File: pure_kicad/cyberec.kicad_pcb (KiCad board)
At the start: 4 copper layers, 50 x 50 mm, 89 parts, among them J1 XT60M, J2 XT60M, J3 XT60M, J4 XT60M, J5 Conn_01x04_Pin, J6 Conn_01x04_Pin, Q1 Q_NMOS_DGS, Q2 Q_NMOS_DGS, Q3 Q_NMOS_DGS, Q4 Q_NMOS_DGS, Q5 Q_PMOS_SGD, Q6 Q_NMOS_DGS, Q7 Q_NMOS_DGS, U1 BQ25756ERRVR, U2 BQ40Z80RSMR

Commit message: Layout starting to look alright
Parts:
- C15, C19, C20, C21, C22, C29, C30, C31, C32, C33, C7, D10, R18, R29: moved to B.Cu
- D9, R26, R27, R28: moved to F.Cu
- R16: footprint Resistor_SMD:R_0402_1005Metric_Pad0.72x0.64mm_HandSolder -> Resistor_SMD:R_0603_1608Metric_Pad0.98x0.95mm_HandSolder
- moved C24 54.5 mm to (81.0, 94.7)
- moved C28 51.7 mm to (81.1, 79.7)
- moved C23 51.3 mm to (81.0, 97.7)
- moved C27 50.0 mm to (81.0, 82.7)
- moved J5 49.1 mm to (77.8, 99.2), turned to 90 degrees
- moved C25 48.8 mm to (81.0, 91.7)
- moved C15 48.4 mm to (96.6, 92.8), turned to 180 degrees
- moved C26 47.4 mm to (81.0, 88.7)
- moved J3 45.5 mm to (121.6, 94.6)
- moved J4 45.5 mm to (121.6, 78.4)
- moved J6 44.8 mm to (77.8, 85.2), turned to 90 degrees
- moved R19 43.4 mm to (81.1, 99.2)
- moved C31 41.2 mm to (85.0, 92.7), turned to 90 degrees
- moved R25 41.0 mm to (81.1, 81.2)
- moved R20 41.0 mm to (81.1, 96.2)
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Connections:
- C15 pad 1: unconnected-(C15-Pad1) -> VAC
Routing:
- net VAC: track 0.00 -> 17.3 mm
- net /Charger/SRN: track 0.00 -> 15.0 mm
- net /Charger/SRP: track 0.00 -> 14.3 mm
- net Net-(U2-VC2): track 0.00 -> 14.1 mm
- net Net-(U2-VC6): track 0.00 -> 14.0 mm
- net Net-(U2-VC5): track 0.00 -> 13.5 mm
- net /Charger/ACP: track 0.00 -> 13.5 mm
- net Net-(U2-VC1): track 0.00 -> 13.3 mm
- net /Charger/ACN: track 0.00 -> 12.2 mm
- net Net-(U2-VC4): track 0.00 -> 11.7 mm
- net Net-(U2-VC3): track 0.00 -> 10.4 mm
- net /Charger/SW1: track 0.00 -> 8.85 mm
- net /Battery Monitor/LED_A: track 0.00 -> 8.22 mm
- net /Charger/FBG: track 0.00 -> 7.86 mm
- net Net-(U2-BAT): track 0.00 -> 7.67 mm
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- added copper zone on In1.Cu, net Earth

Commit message: Do most top side zones
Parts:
- C1, C10, C15, C18, C19, C2, C20, C21, C22, C23, C24, C25, C26, C27, C28, C29, C3, C30, C31, C32, C33, C4, C5, C6, C7, C8, C9: footprint Capacitor_SMD:C_0603_1608Metric_Pad1.08x0.95mm_HandSolder -> cyberec:C_0603_1608Metric_Pad1.08x0.95mm_HandSolder
- C11, C12, C14, C16, C17: footprint Capacitor_SMD:CP_Elec_10x14.3 -> cyberec:CP_Elec_10x14.3
- C13, C34: footprint Capacitor_SMD:C_0603_1608Metric_Pad1.08x0.95mm_HandSolder -> cyberec:C_0603_1608Metric_Pad1.08x0.95mm_HandSolder; moved to B.Cu
- D1, D2: footprint Diode_SMD:D_SMA_Handsoldering -> cyberec:D_SOD-882D
- D10: footprint Diode_SMD:D_SMA_Handsoldering -> cyberec:D_SMA_Handsoldering; moved to F.Cu
- D3, D4, D5, D6, D7, D8: footprint LED_SMD:LED_0603_1608Metric_Pad1.05x0.95mm_HandSolder -> cyberec:LED_0603_1608Metric_Pad1.05x0.95mm_HandSolder
- D9: footprint Diode_SMD:D_SMA_Handsoldering -> cyberec:D_SMA_Handsoldering
- J1, J2, J3, J4: footprint Connector_AMASS:AMASS_XT60-M_1x02_P7.20mm_Vertical -> cyberec:AMASS_XT60-M_1x02_P7.20mm_Vertical
- J5, J6: footprint Connector_JST:JST_XH_B4B-XH-A_1x04_P2.50mm_Vertical -> cyberec:JST_XH_B4B-XH-A_1x04_P2.50mm_Vertical
- R1, R10, R11, R12, R13, R15, R16, R18, R19, R2, R20, R21, R23, R24, R25, R29, R5, R6, R7, R8, R9: footprint Resistor_SMD:R_0603_1608Metric_Pad0.98x0.95mm_HandSolder -> cyberec:R_0603_1608Metric_Pad0.98x0.95mm_HandSolder
- R14, R26, R27, R28: footprint Resistor_SMD:R_0402_1005Metric_Pad0.72x0.64mm_HandSolder -> cyberec:R_0402_1005Metric_Pad0.72x0.64mm_HandSolder
- R22: footprint Resistor_SMD:R_1210_3225Metric_Pad1.30x2.65mm_HandSolder -> cyberec:R_1210_3225Metric_Pad1.30x2.65mm_HandSolder
- moved D9 21.3 mm to (112.2, 104.2), turned to 180 degrees
- moved C34 19.9 mm to (88.5, 89.8), turned to 180 degrees
- moved D10 17.7 mm to (115.2, 90.8), turned to -90 degrees
- moved C13 11.2 mm to (94.5, 86.6)
- moved R5 9.06 mm to (82.8, 103.6), turned to 0 degrees
- moved R22 8.84 mm to (110.5, 88.2), turned to 0 degrees
- moved R1 8.68 mm to (82.8, 105.4), turned to 0 degrees
- moved C3 5.02 mm to (85.5, 104.5), turned to 90 degrees
- moved R27 3.25 mm to (112.8, 93.5)
- moved R26 2.90 mm to (112.8, 96.8)
- moved C5 2.74 mm to (88.3, 103.6), turned to 0 degrees
- moved Q6 2.30 mm to (115.2, 98.7)
- moved Q5 2.30 mm to (110.4, 93.5)
- moved Q7 2.30 mm to (110.2, 99.0)
- moved R28 1.25 mm to (112.8, 101.0)
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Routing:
- net /Charger/ACP: track 13.5 -> 0.00 mm
- net /Charger/ACN: track 12.2 -> 0.00 mm
- net /Charger/SW1: track 8.85 -> 0.00 mm
- net VAC: track 17.3 -> 25.6 mm
- net /Battery Monitor/DSG: track 0.00 -> 6.24 mm
- net VCC: track 0.00 -> 4.19 mm
- net /Battery Monitor/CHG: track 0.00 -> 3.62 mm
- net /Battery Monitor/PCHG: track 0.00 -> 1.83 mm
- net Net-(D10-K): track 1.27 -> 0.00 mm
- net Net-(C1-Pad2): track 4.72 -> 3.75 mm
- net Net-(C3-Pad2): track 4.68 -> 3.75 mm
- net Net-(C2-Pad2): track 4.39 -> 3.50 mm
- net Net-(C4-Pad2): track 4.29 -> 3.50 mm
- net Earth: vias 0 -> 6
- added copper zone on F.Cu, net +BATT
- added copper zone on F.Cu, net /Charger/SW1
- added copper zone on F.Cu, net /Charger/SW2
- added copper zone on F.Cu, net Earth
- added copper zone on F.Cu, net Net-(Q5-D)
- added copper zone on F.Cu, net VAC
- added copper zone on F.Cu, net VCC
- added copper zone on F.Cu, net VDD
- added copper zone on F.Cu, net VDDA
- added copper zone on F.Cu, net VDDF
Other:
- outline, holes or cut-outs redrawn

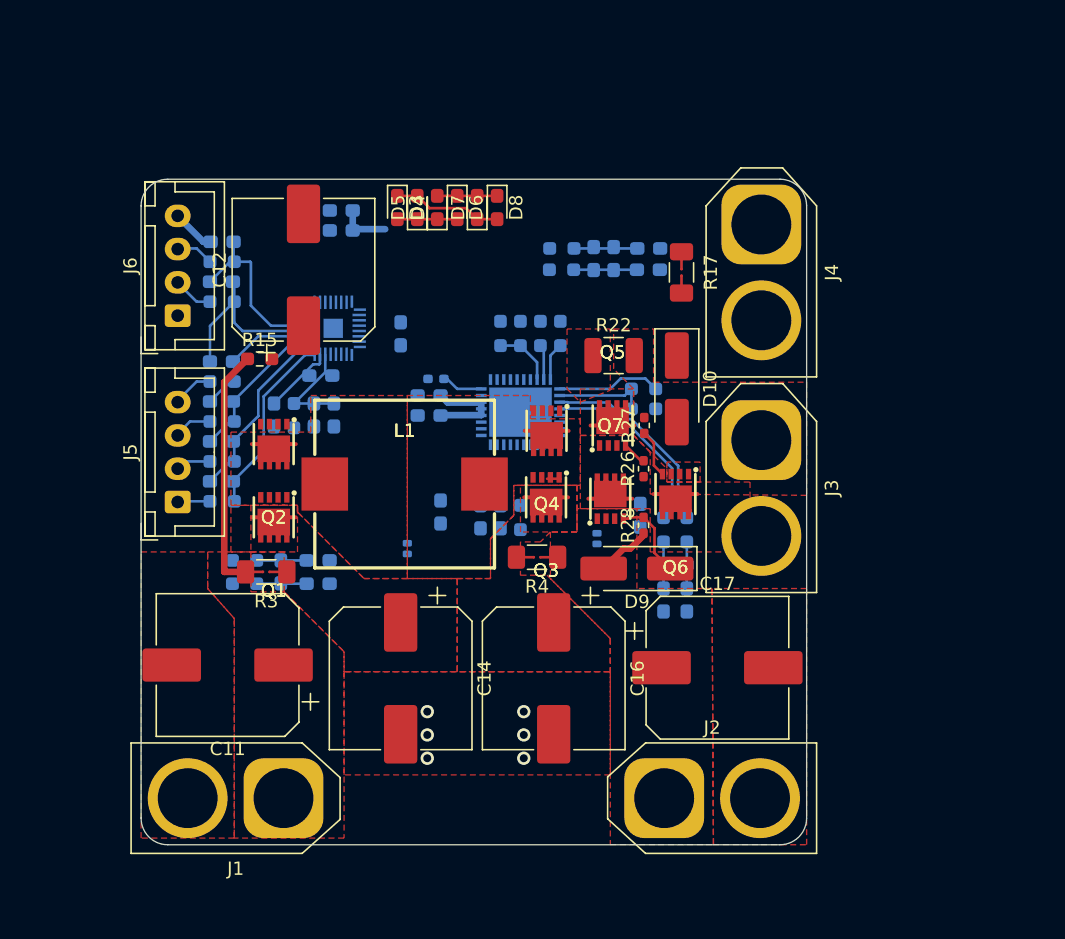
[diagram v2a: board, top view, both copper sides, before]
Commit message: It seems that the charger needs to move.
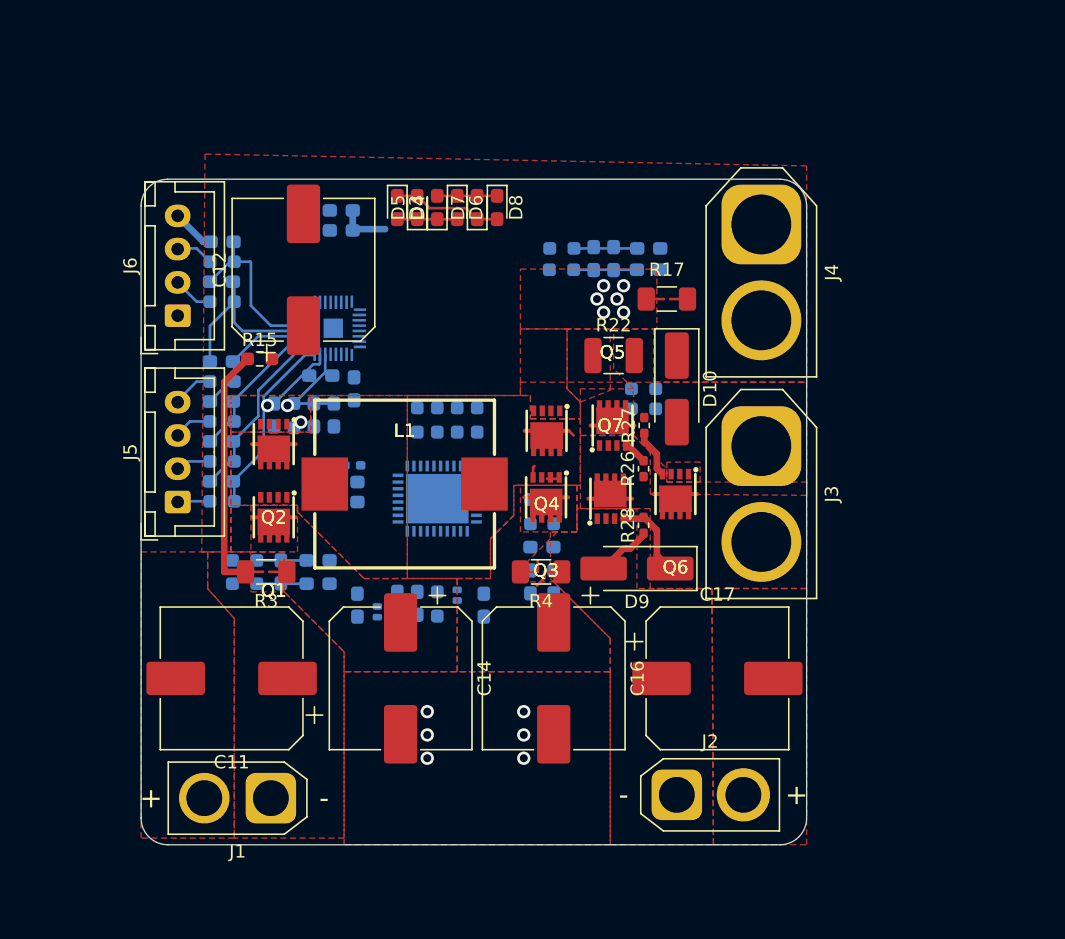
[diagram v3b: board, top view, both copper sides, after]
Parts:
- D1, D2: value D_Schottky -> PMEG2010BELD
- J1: value XT60M -> XT30M; footprint cyberec:AMASS_XT60-M_1x02_P7.20mm_Vertical -> cyberec:AMASS_XT30U-M_1x02_P5.0mm_Vertical
- J2: value XT60M -> XT30F; footprint cyberec:AMASS_XT60-M_1x02_P7.20mm_Vertical -> cyberec:AMASS_XT30U-F_1x02_P5.0mm_Vertical
- moved C8 13.6 mm to (100.8, 107.0)
- moved D2 11.3 mm to (98.8, 106.2), turned to 90 degrees
- moved R2 10.1 mm to (104.2, 100.0)
- moved R6 10.1 mm to (106.0, 100.0)
- moved C2 10.1 mm to (104.2, 105.2)
- moved C4 10.1 mm to (105.1, 102.6)
- moved C6 10.1 mm to (106.0, 105.2)
- moved C7 9.38 mm to (91.2, 107.0), turned to -90 degrees
- moved C10 9.02 mm to (94.2, 106.9)
- moved C15 9.02 mm to (90.4, 99.2)
- moved C18 9.02 mm to (90.4, 97.8)
- moved C9 9.02 mm to (95.8, 106.9)
- moved R10 9.02 mm to (97.2, 93.1)
- moved R13 9.02 mm to (97.2, 106.9)
- moved R14 9.02 mm to (90.9, 96.5)
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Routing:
- net /Charger/SRN: track 15.0 -> 0.00 mm
- net /Charger/SRP: track 14.3 -> 0.00 mm
- net /Charger/FBG: track 7.86 -> 0.00 mm
- net VAC: track 25.6 -> 18.3 mm
- net /Charger/FB: track 7.10 -> 0.00 mm
- net TS_Charge: track 4.57 -> 0.00 mm
- net Net-(U1B-FSW_SYNC): track 3.12 -> 0.00 mm
- net Net-(U1A-ILIM_HIZ): track 2.86 -> 0.00 mm
- net Net-(C2-Pad2): track 3.50 -> 0.83 mm
- net Net-(U1A-ICHG): track 2.66 -> 0.00 mm
- net Net-(C4-Pad2): track 3.50 -> 1.28 mm
- net /Charger/HIDRV2: track 0.00 -> 0.90 mm
- net /Charger/SW2: track 1.02 -> 1.89 mm
- net Net-(D10-K): vias 0 -> 1
- net Earth: vias 6 -> 14
- added copper zone on F.Cu, net -BATT

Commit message: So, 10u X5Rs are a thing. Just use 40 of them
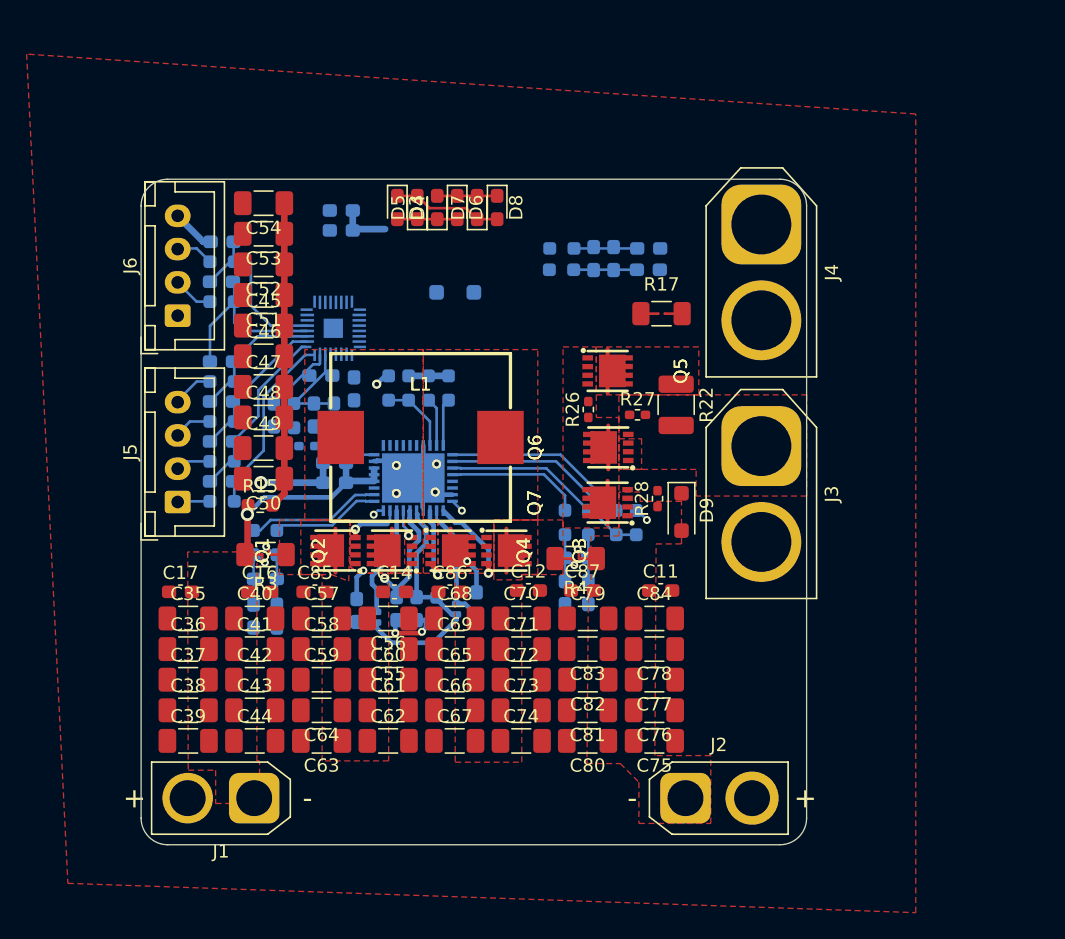
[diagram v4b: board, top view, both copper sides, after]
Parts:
- added C35: 10uF, cyberec:C_1206_3216Metric_Pad1.33x1.80mm_HandSolder, F.Cu at (78.5, 108.0)
- added C36: 10uF, cyberec:C_1206_3216Metric_Pad1.33x1.80mm_HandSolder, F.Cu at (78.5, 110.3)
- added C37: 10uF, cyberec:C_1206_3216Metric_Pad1.33x1.80mm_HandSolder, F.Cu at (78.5, 112.6)
- added C38: 10uF, cyberec:C_1206_3216Metric_Pad1.33x1.80mm_HandSolder, F.Cu at (78.5, 114.9)
- added C39: 10uF, cyberec:C_1206_3216Metric_Pad1.33x1.80mm_HandSolder, F.Cu at (78.5, 117.2)
- added C40: 10uF, cyberec:C_1206_3216Metric_Pad1.33x1.80mm_HandSolder, F.Cu at (83.5, 108.0)
- added C41: 10uF, cyberec:C_1206_3216Metric_Pad1.33x1.80mm_HandSolder, F.Cu at (83.5, 110.3)
- added C42: 10uF, cyberec:C_1206_3216Metric_Pad1.33x1.80mm_HandSolder, F.Cu at (83.5, 112.6)
- added C43: 10uF, cyberec:C_1206_3216Metric_Pad1.33x1.80mm_HandSolder, F.Cu at (83.5, 114.9)
- added C44: 10uF, cyberec:C_1206_3216Metric_Pad1.33x1.80mm_HandSolder, F.Cu at (83.5, 117.2)
- added C45: 10uF, cyberec:C_1206_3216Metric_Pad1.33x1.80mm_HandSolder, F.Cu at (84.2, 86.0)
- added C46: 10uF, cyberec:C_1206_3216Metric_Pad1.33x1.80mm_HandSolder, F.Cu at (84.2, 88.3)
- added C47: 10uF, cyberec:C_1206_3216Metric_Pad1.33x1.80mm_HandSolder, F.Cu at (84.2, 90.6)
- added C48: 10uF, cyberec:C_1206_3216Metric_Pad1.33x1.80mm_HandSolder, F.Cu at (84.2, 92.9)
- added C49: 10uF, cyberec:C_1206_3216Metric_Pad1.33x1.80mm_HandSolder, F.Cu at (84.2, 95.2)
- added C50: 10uF, cyberec:C_1206_3216Metric_Pad1.33x1.80mm_HandSolder, F.Cu at (84.2, 97.5)
- added C51: 10uF, cyberec:C_1206_3216Metric_Pad1.33x1.80mm_HandSolder, F.Cu at (84.2, 83.7)
- added C52: 10uF, cyberec:C_1206_3216Metric_Pad1.33x1.80mm_HandSolder, F.Cu at (84.2, 81.4)
- added C53: 10uF, cyberec:C_1206_3216Metric_Pad1.33x1.80mm_HandSolder, F.Cu at (84.2, 79.1)
- added C54: 10uF, cyberec:C_1206_3216Metric_Pad1.33x1.80mm_HandSolder, F.Cu at (84.2, 76.8)
- added C55: 10uF, cyberec:C_1206_3216Metric_Pad1.33x1.80mm_HandSolder, F.Cu at (93.6, 110.3)
- added C56: 10uF, cyberec:C_1206_3216Metric_Pad1.33x1.80mm_HandSolder, F.Cu at (93.6, 108.0)
- added C57: 10uF, cyberec:C_1206_3216Metric_Pad1.33x1.80mm_HandSolder, F.Cu at (88.6, 108.0)
- added C58: 10uF, cyberec:C_1206_3216Metric_Pad1.33x1.80mm_HandSolder, F.Cu at (88.6, 110.3)
- added C59: 10uF, cyberec:C_1206_3216Metric_Pad1.33x1.80mm_HandSolder, F.Cu at (88.6, 112.6)
- added C60: 10uF, cyberec:C_1206_3216Metric_Pad1.33x1.80mm_HandSolder, F.Cu at (93.6, 112.6)
- added C61: 10uF, cyberec:C_1206_3216Metric_Pad1.33x1.80mm_HandSolder, F.Cu at (93.6, 114.9)
- added C62: 10uF, cyberec:C_1206_3216Metric_Pad1.33x1.80mm_HandSolder, F.Cu at (93.6, 117.2)
- added C63: 10uF, cyberec:C_1206_3216Metric_Pad1.33x1.80mm_HandSolder, F.Cu at (88.6, 117.2)
- added C64: 10uF, cyberec:C_1206_3216Metric_Pad1.33x1.80mm_HandSolder, F.Cu at (88.6, 114.9)
- added C65: 10uF, cyberec:C_1206_3216Metric_Pad1.33x1.80mm_HandSolder, F.Cu at (98.6, 112.6)
- added C66: 10uF, cyberec:C_1206_3216Metric_Pad1.33x1.80mm_HandSolder, F.Cu at (98.6, 114.9)
- added C67: 10uF, cyberec:C_1206_3216Metric_Pad1.33x1.80mm_HandSolder, F.Cu at (98.6, 117.2)
- added C68: 10uF, cyberec:C_1206_3216Metric_Pad1.33x1.80mm_HandSolder, F.Cu at (98.6, 108.0)
- added C69: 10uF, cyberec:C_1206_3216Metric_Pad1.33x1.80mm_HandSolder, F.Cu at (98.6, 110.3)
- added C70: 10uF, cyberec:C_1206_3216Metric_Pad1.33x1.80mm_HandSolder, F.Cu at (103.6, 108.0)
- added C71: 10uF, cyberec:C_1206_3216Metric_Pad1.33x1.80mm_HandSolder, F.Cu at (103.6, 110.3)
- added C72: 10uF, cyberec:C_1206_3216Metric_Pad1.33x1.80mm_HandSolder, F.Cu at (103.6, 112.6)
- added C73: 10uF, cyberec:C_1206_3216Metric_Pad1.33x1.80mm_HandSolder, F.Cu at (103.6, 114.9)
- added C74: 10uF, cyberec:C_1206_3216Metric_Pad1.33x1.80mm_HandSolder, F.Cu at (103.6, 117.2)
- added C75: 10uF, cyberec:C_1206_3216Metric_Pad1.33x1.80mm_HandSolder, F.Cu at (113.6, 117.2)
- added C76: 10uF, cyberec:C_1206_3216Metric_Pad1.33x1.80mm_HandSolder, F.Cu at (113.6, 114.9)
- added C77: 10uF, cyberec:C_1206_3216Metric_Pad1.33x1.80mm_HandSolder, F.Cu at (113.6, 112.6)
- added C78: 10uF, cyberec:C_1206_3216Metric_Pad1.33x1.80mm_HandSolder, F.Cu at (113.6, 110.3)
- added C79: 10uF, cyberec:C_1206_3216Metric_Pad1.33x1.80mm_HandSolder, F.Cu at (108.6, 108.0)
- added C80: 10uF, cyberec:C_1206_3216Metric_Pad1.33x1.80mm_HandSolder, F.Cu at (108.5, 117.2)
- added C81: 10uF, cyberec:C_1206_3216Metric_Pad1.33x1.80mm_HandSolder, F.Cu at (108.5, 114.9)
- added C82: 10uF, cyberec:C_1206_3216Metric_Pad1.33x1.80mm_HandSolder, F.Cu at (108.6, 112.6)
- added C83: 10uF, cyberec:C_1206_3216Metric_Pad1.33x1.80mm_HandSolder, F.Cu at (108.5, 110.3)
- added C84: 10uF, cyberec:C_1206_3216Metric_Pad1.33x1.80mm_HandSolder, F.Cu at (113.6, 108.0)
- added C85: 100nF, cyberec:C_0603_1608Metric_Pad1.08x0.95mm_HandSolder, F.Cu at (88.1, 106.0)
- added C86: 100nF, cyberec:C_0603_1608Metric_Pad1.08x0.95mm_HandSolder, F.Cu at (98.2, 106.0)
- added C87: 100nF, cyberec:C_0603_1608Metric_Pad1.08x0.95mm_HandSolder, F.Cu at (108.2, 105.9)
- C11, C12, C14, C16: value 82uF -> 1uF; footprint cyberec:CP_Elec_10x14.3 -> cyberec:C_0603_1608Metric_Pad1.08x0.95mm_HandSolder
- C17: value 82uF -> 100nF; footprint cyberec:CP_Elec_10x14.3 -> cyberec:C_0603_1608Metric_Pad1.08x0.95mm_HandSolder
- D10: value D_Schottky -> 1N4001; footprint cyberec:D_SMA_Handsoldering -> Diode_SMD:D_SOD-123F; moved to B.Cu
- D9: value D_Schottky -> 1N4001; footprint cyberec:D_SMA_Handsoldering -> Diode_SMD:D_SOD-123F
- moved C17 40.9 mm to (78.0, 106.0)
- moved C11 32.9 mm to (114.0, 105.9), turned to 0 degrees
- moved C12 29.4 mm to (104.1, 105.9), turned to 0 degrees
- moved C16 23.0 mm to (83.9, 106.0), turned to 0 degrees
- moved D10 18.2 mm to (98.6, 83.5), turned to 180 degrees
- moved Q2 12.0 mm to (93.8, 102.9), turned to 90 degrees
- moved Q4 11.5 mm to (98.2, 102.9), turned to -90 degrees
- moved R15 11.0 mm to (84.0, 99.5)
- moved R12 10.3 mm to (110.7, 100.8), turned to 90 degrees
- moved R11 8.57 mm to (112.2, 100.8), turned to -90 degrees
- moved C14 6.52 mm to (94.0, 106.0), turned to 0 degrees
- moved Q6 6.14 mm to (110.1, 95.2), turned to 90 degrees
- moved R26 6.08 mm to (108.6, 92.3)
- moved R22 5.98 mm to (115.2, 92.0), turned to -90 degrees
- moved C1 5.43 mm to (83.5, 107.8), turned to 90 degrees
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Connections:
- C11 pad 1: VAC -> VCC
- C12 pad 1: Net-(C12-Pad1) -> VDDA
- C16 pad 1: VDDA -> VAC
- C17 pad 1: VCC -> Earth
- C17 pad 2: Earth -> VAC
- R15 pad 2: Net-(C12-Pad1) -> Net-(C45-Pad2)
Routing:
- net Earth: track 0.00 -> 29.1 mm, vias 14 -> 7
- net /Charger/REGN: track 0.00 -> 25.3 mm, vias 0 -> 2
- net Net-(C45-Pad2): track 0.00 -> 23.1 mm
- net /Charger/DRV_SUP: track 0.00 -> 18.5 mm
- net /Charger/FB: track 0.00 -> 16.7 mm
- net /Charger/FBG: track 0.00 -> 14.0 mm
- net /Charger/SRN: track 0.00 -> 11.5 mm
- net /Charger/BTST1: track 0.00 -> 10.3 mm
- net /Charger/SRP: track 0.00 -> 10.2 mm
- net /Charger/ACP: track 0.00 -> 10.2 mm
- net /Charger/BTST2: track 0.00 -> 9.48 mm
- net /Charger/ACN: track 0.00 -> 8.23 mm
- net /Charger/HIDRV2: track 0.90 -> 7.17 mm, vias 0 -> 1
- net /Battery Monitor/DSG: track 6.17 -> 0.00 mm
- net /Charger/LODRV2: track 0.00 -> 6.13 mm, vias 0 -> 1
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- removed copper zone on F.Cu, net -BATT
